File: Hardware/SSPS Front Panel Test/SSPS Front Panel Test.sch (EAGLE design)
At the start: 81 parts, among them J1 61400413321, SW1 B3W-9000-RG2C, SW2 B3W-9000-RG2C, U1 P8X32A-Q44, U10 STP16CP05XTTR, U11 FT230XS, U12 IP4234CZ6, U2 STP16CP05XTTR, U3 STP16CP05XTTR, U4 STP16CP05XTTR, U5 STP16CP05XTTR, U6 STP16CP05XTTR, U7 AP1084D25G-13, U8 AP1084D33G-13, U9 STP16CP05XTTR

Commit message: Test for Front Panel of SSPS complete.
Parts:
- removed DISP21: CU16025-UWJ6, PP_Displays:CU16025-UWJ6
- removed H1, H2, H3, H4: MOUNT_HOLE150MIL, PP_Connectors:MOUNT_HOLE150MIL
- added 5V: 5000, PP_Connectors:TEST_POINT_SINGLE_KEYSTONE_5115-5119
- added C17, C18, C19, C20, C21, C22, C23: .1uF, PP_Passives:CAPACITOR_NON_POLAR_0603
- added C24, C25, C26: 0.1uF, PP_Passives:CAPACITOR_NON_POLAR_0603
- added FID1, FID2: FIDUCIAL_100MIL, MF_Aesthetics:FIDUCIAL_100MIL
- added FRAME1: MF_FRAMEDEFAULT, MF_Aesthetics:MF_FRAMEDEFAULT
- added GND: 5001, PP_Connectors:TEST_POINT_SINGLE_KEYSTONE_5115-5119
- added J2: (no value), PP_Connectors:CON_01X08_2.54MM_PIN_HEADER
- added LCD1: CU16025-UW6J, PP_Displays:CU16025-UWJ6
- added R12, R13, R14, R16, R17, R18, R19, R20, R21, R22: 10K, PP_Passives:RESISTOR_0603
- added R15: 1K, PP_Passives:RESISTOR_0603
- added SW3: 5501, PP_Electromechanical:5501
- added U13: FT234XD-R, PP_DigitalIC:FT234XD
- added U14: STP16CP05XTTR, PP_DigitalIC:STP16CP05XTTR
- added X1: ABMM-6.000MHZ-B2-T, MF_Frequency_Control:XTL_7MMX5MM
- U1: value P8X32A-Q44 -> P8X32A-M44; device MF_IC_Digital:P8X32A-Q44 -> PP_DigitalIC:P8X32A-M44
- U11: value FT230XS -> CAT24C512WI-GT3; device MF_IC_Digital:FT230XS -> PP_DigitalIC:EEPROM_I2CSOIC-8_W
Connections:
- removed net RX_LED: U11.CBUS1
- removed net TX_LED: U11.CBUS0
- new net DISP9_DATA: U14.SDO
- new net ENCODER_A: C25.1, R18.2, U1.P7
- new net ENCODER_B: C26.1, R19.1, U1.P6
- new net LCD_SCK: LCD1.SCK, U1.P2
- new net LCD_SI/SO: LCD1.SI/SO, U1.P0
- new net LCD_STB: LCD1.STB, U1.P1
- new net N$39: R15.2, U14.R-EXT
- new net N$40: EN1.1, U14.!OUT0
- new net N$41: EN1.2, U14.!OUT1
- new net N$42: EN1.4, U14.!OUT2
- new net N$43: SW1.CATHODE_1, U14.!OUT3
- new net N$44: SW1.CATHODE_2, U14.!OUT4
- new net N$45: SW2.CATHODE_1, U14.!OUT5
- new net N$46: SW2.CATHODE_2, U14.!OUT6
- new net N$47: SW3.CATHODE_1, U14.!OUT7
- new net N$48: SW3.CATHODE_2, U14.!OUT8
- new net N$49: R20.2, SW1.3
- new net N$50: R21.2, SW2.3
- new net N$54: R22.2, SW3.2
- new net P11: J2.1, U1.P11
- new net P12: J2.2, U1.P12
- new net P13: J2.3, U1.P13
- new net P14: J2.4, U1.P14
- new net P15: J2.5, U1.P15
- new net P16: J2.6, U1.P16
- new net P17: J2.7, U1.P17
- new net P18: J2.8, U1.P18
- new net P19: U1.P19
- new net P20: U1.P20
- new net P21: U1.P21
- new net P22: U1.P22
- new net P23: U1.P23
- new net P24: U1.P24
- new net P25: U1.P25
- new net P26: U1.P26
- new net P27: U1.P27
- new net RES: C21.1, R14.1, U1.!RES
- new net SCL: R12.1, U1.P28, U11.SCL
- new net SDA: R13.1, U1.P29, U11.SDA
- new net SW_1: SW1.4, U1.P8
- new net SW_2: SW2.4, U1.P9
- new net SW_3: SW3.3, U1.P10
- new net TERMINAL_A: EN1.A, R16.1, R18.1
- new net TERMINAL_B: EN1.B, R17.1, R19.2
- new net USB_RST: C21.2
- new net X0: U1.X0, X1.X1
- new net X1: U1.X1, X1.X0
- net 2.5V: now also EN1.5, SW1.ANODE_1, SW1.ANODE_2, SW2.ANODE_1, SW2.ANODE_2, SW3.ANODE_1, SW3.ANODE_2
- net 3.3V: now also C17.2, C18.2, C19.2, C20.2, C22.2, C23.2, C24.1, R12.2, R13.2, R14.2, R16.2, R17.2, R20.1, R21.1, R22.1, U1.VDD, U13.VCC, U14.VDD
- net 3V3OUT: now also U13.3V3OUT, U13.RESET#, U13.VCCIO; no longer U11.!RESET, U11.3V3OUT, U11.VCCIO
- net DISP1_DATA: now also U1.P5
- net DISP8_DATA: now also U14.SDI
- net DISPX_CLK: now also U1.P3, U14.CLK
- net DISPX_LAT: now also U1.P4, U14.LE/DM1
- net GND: now also C17.1, C18.1, C19.1, C20.1, C22.1, C23.1, C24.2, C25.2, C26.2, EN1.C, GND.P$1, LCD1.GND2, R15.1, SW1.1, SW2.1, SW3.1A, U1.!BOE, U1.VSS, U11.A0, U11.A1, U11.A2, U11.WP, U13.GND, U14.!OE/DM2, U14.VSS/GND, X1.GND
- net N$34: now also U13.USBDM; no longer U11.USBDM
- net N$36: now also U13.USBDP; no longer U11.USBDP
- net RX: now also U1.P30, U13.RXD; no longer U11.RXD
- net TX: now also U1.P31, U13.TXD; no longer U11.TXD
- net USB_!RST: now also U13.RTS#; no longer U11.!RTS
- net VBUS_SENSE: now also U13.CBUS0; no longer U11.CBUS3
- net VIN: now also 5V.P$1, LCD1.VCC2
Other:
- moved on the sheet: EN1, SW1, SW2, U1

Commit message: Fixed part numbers.
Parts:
- DISP2, DISP3, DISP4, DISP5: value PSA08-11GWA -> PSA08-11SRWA
- SW3: value 5501 -> 5501M112
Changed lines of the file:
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@@
 <grid distance="0.1" unitdist="inch" unit="inch" style="lines" multiple="1" display="no" altdistance="0.01" altunitdist="inch" altunit="inch"/>
 <layers>
-<layer number="1" name="Top" color="4" fill="1" visible="yes" active="no"/>
-<layer number="2" name="Route2" color="1" fill="3" visible="yes" active="no"/>
-<layer number="3" name="Route3" color="4" fill="3" visible="yes" active="no"/>
-<layer number="4" name="Route4" color="1" fill="4" visible="yes" active="no"/>
-<layer number="5" name="Route5" color="4" fill="4" visible="yes" active="no"/>
-<layer number="6" name="Route6" color="1" fill="8" visible="yes" active="no"/>
-<layer number="7" name="Route7" color="4" fill="8" visible="yes" active="no"/>
-<layer number="8" name="Route8" color="1" fill="2" visible="yes" active="no"/>
-<layer number="9" name="Route9" color="4" fill="2" visible="yes" active="no"/>
-<layer number="10" name="Route10" color="1" fill="7" visible="yes" active="no"/>
-<layer number="11" name="Route11" color="4" fill="7" visible="yes" active="no"/>
-<layer number="12" name="Route12" color="1" fill="5" visible="yes" active="no"/>
-<layer number="13" name="Route13" color="4" fill="5" visible="yes" active="no"/>
-<layer number="14" name="Route14" color="1" fill="6" visible="yes" active="no"/>
-<layer number="15" name="Route15" color="4" fill="6" visible="yes" active="no"/>
-<layer number="16" name="Bottom" color="1" fill="1" visible="yes" active="no"/>
-<layer number="17" name="Pads" color="2" fill="1" visible="yes" active="no"/>
-<layer number="18" name="Vias" color="2" fill="1" visible="yes" active="no"/>
-<layer number="19" name="Unrouted" color="6" fill="1" visible="yes" active="no"/>
-<layer number="20" name="Dimension" color="15" fill="1" visible="yes" active="no"/>
-<layer number="21" name="tPlace" color="7" fill="1" visible="yes" active="no"/>
-<layer number="22" name="bPlace" color="7" fill="1" visible="yes" active="no"/>
-<layer number="23" name="tOrigins" color="15" fill="1" visible="yes" active="no"/>
-<layer number="24" name="bOrigins" color="15" fill="1" visible="yes" active="no"/>
-<layer number="25" name="tNames" color="7" fill="1" visible="yes" active="no"/>
-<layer number="26" name="bNames" color="7" fill="1" visible="yes" active="no"/>
-<layer number="27" name="tValues" color="7" fill="1" visible="yes" active="no"/>
-<layer number="28" name="bValues" color="7" fill="1" visible="yes" active="no"/>
+<layer number="1" name="Top" color="4" fill="1" visible="no" active="no"/>
+<layer number="2" name="Route2" color="1" fill="3" visible="no" active="no"/>
+<layer number="3" name="Route3" color="4" fill="3" visible="no" active="no"/>
+<layer number="4" name="Route4" color="1" fill="4" visible="no" active="no"/>
+<layer number="5" name="Route5" color="4" fill="4" visible="no" active="no"/>
+<layer number="6" name="Route6" color="1" fill="8" visible="no" active="no"/>
+<layer number="7" name="Route7" color="4" fill="8" visible="no" active="no"/>
+<layer number="8" name="Route8" color="1" fill="2" visible="no" active="no"/>
+<layer number="9" name="Route9" color="4" fill="2" visible="no" active="no"/>
+<layer number="10" name="Route10" color="1" fill="7" visible="no" active="no"/>
+<layer number="11" name="Route11" color="4" fill="7" visible="no" active="no"/>
+<layer number="12" name="Route12" color="1" fill="5" visible="no" active="no"/>
+<layer number="13" name="Route13" color="4" fill="5" visible="no" active="no"/>
+<layer number="14" name="Route14" color="1" fill="6" visible="no" active="no"/>
+<layer number="15" name="Route15" color="4" fill="6" visible="no" active="no"/>
+<layer number="16" name="Bottom" color="1" fill="1" visible="no" active="no"/>
+<layer number="17" name="Pads" color="2" fill="1" visible="no" active="no"/>
+<layer number="18" name="Vias" color="2" fill="1" visible="no" active="no"/>
+<layer number="19" name="Unrouted" color="6" fill="1" visible="no" active="no"/>
+<layer number="20" name="Dimension" color="15" fill="1" visible="no" active="no"/>
+<layer number="21" name="tPlace" color="7" fill="1" visible="no" active="no"/>
+<layer number="22" name="bPlace" color="7" fill="1" visible="no" active="no"/>
+<layer number="23" name="tOrigins" color="15" fill="1" visible="no" active="no"/>
+<layer number="24" name="bOrigins" color="15" fill="1" visible="no" active="no"/>
+<layer number="25" name="tNames" color="7" fill="1" visible="no" active="no"/>
+<layer number="26" name="bNames" color="7" fill="1" visible="no" active="no"/>
+<layer number="27" name="tValues" color="7" fill="1" visible="no" active="no"/>
+<layer number="28" name="bValues" color="7" fill="1" visible="no" active="no"/>
 <layer number="29" name="tStop" color="7" fill="3" visible="no" active="no"/>
 <layer number="30" name="bStop" color="7" fill="6" visible="no" active="no"/>
@@
 <layer number="35" name="tGlue" color="7" fill="4" visible="no" active="no"/>
 <layer number="36" name="bGlue" color="7" fill="5" visible="no" active="no"/>
-<layer number="37" name="tTest" color="7" fill="1" visible="yes" active="no"/>
-<layer number="38" name="bTest" color="7" fill="1" visible="yes" active="no"/>
+<layer number="37" name="tTest" color="7" fill="1" visible="no" active="no"/>
+<layer number="38" name="bTest" color="7" fill="1" visible="no" active="no"/>
 <layer number="39" name="tKeepout" color="4" fill="11" visible="no" active="no"/>
 <layer number="40" name="bKeepout" color="1" fill="11" visible="no" active="no"/>
@@
 <layer number="44" name="Drills" color="7" fill="1" visible="no" active="no"/>
 <layer number="45" name="Holes" color="7" fill="1" visible="no" active="no"/>
-<layer number="46" name="Milling" color="3" fill="1" visible="yes" active="no"/>
-<layer number="47" name="Measures" color="7" fill="1" visible="yes" active="no"/>
-<layer number="48" name="Document" color="7" fill="1" visible="yes" active="no"/>
-<layer number="49" name="Reference" color="7" fill="1" visible="yes" active="no"/>
-<layer number="50" name="dxf" color="7" fill="1" visible="yes" active="no"/>
-<layer number="51" name="tDocu" color="7" fill="1" visible="yes" active="no"/>
-<layer number="52" name="bDocu" color="7" fill="1" visible="yes" active="no"/>
-<layer number="53" name="tGND_GNDA" color="7" fill="9" visible="yes" active="no"/>
-<layer number="54" name="bGND_GNDA" color="1" fill="9" visible="yes" active="no"/>
-<layer number="56" name="wert" color="7" fill="1" visible="yes" active="no"/>
+<layer number="46" name="Milling" color="3" fill="1" visible="no" active="no"/>
+<layer number="47" name="Measures" color="7" fill="1" visible="no" active="no"/>
+<layer number="48" name="Document" color="7" fill="1" visible="no" active="no"/>
+<layer number="49" name="Reference" color="7" fill="1" visible="no" active="no"/>
+<layer number="50" name="dxf" color="7" fill="1" visible="no" active="no"/>
+<layer number="51" name="tDocu" color="7" fill="1" visible="no" active="no"/>
+<layer number="52" name="bDocu" color="7" fill="1" visible="no" active="no"/>
+<layer number="53" name="tGND_GNDA" color="7" fill="9" visible="no" active="no"/>
+<layer number="54" name="bGND_GNDA" color="1" fill="9" visible="no" active="no"/>
+<layer number="56" name="wert" color="7" fill="1" visible="no" active="no"/>
 <layer number="91" name="Nets" color="2" fill="1" visible="yes" active="yes"/>
 <layer number="92" name="Busses" color="1" fill="1" visible="yes" active="yes"/>
@@
 <parts>
 <part name="DISP1" library="PP_LED" deviceset="PSA08-11SRWA" device="" value="PSA08-11SRWA"/>
-<part name="DISP2" library="PP_LED" deviceset="PSA08-11SRWA" device="" value="PSA08-11GWA"/>
-<part name="DISP3" library="PP_LED" deviceset="PSA08-11SRWA" device="" value="PSA08-11GWA"/>
-<part name="DISP4" library="PP_LED" deviceset="PSA08-11SRWA" device="" value="PSA08-11GWA"/>
+<part name="DISP2" library="PP_LED" deviceset="PSA08-11SRWA" device="" value="PSA08-11SRWA"/>
+<part name="DISP3" library="PP_LED" deviceset="PSA08-11SRWA" device="" value="PSA08-11SRWA"/>
+<part name="DISP4" library="PP_LED" deviceset="PSA08-11SRWA" device="" value="PSA08-11SRWA"/>
 <part name="D1" library="PP_LED" deviceset="LED_SINGLE" device="_WP1043" value="WP1043ID"/>
 <part name="D2" library="PP_LED" deviceset="LED_SINGLE" device="_WP1043" value="WP1043ID"/>
@@
 <part name="D7" library="PP_LED" deviceset="LED_SINGLE" device="_WP1043" value="WP1043YD"/>
 <part name="D8" library="PP_LED" deviceset="LED_SINGLE" device="_WP1043" value="WP1043YD"/>
-<part name="DISP5" library="PP_LED" deviceset="PSA08-11SRWA" device="" value="PSA08-11GWA"/>
+<part name="DISP5" library="PP_LED" deviceset="PSA08-11SRWA" device="" value="PSA08-11SRWA"/>
 <part name="D9" library="PP_LED" deviceset="LED_SINGLE" device="_WP1043" value="WP1043YD"/>
 <part name="D10" library="PP_LED" deviceset="LED_SINGLE" device="_WP1043" value="WP1043YD"/>
@@
 <part name="5V" library="PP_Connectors" deviceset="TEST_POINT_SINGLE" device="_KEYSTONE_5115-5119" value="5000"/>
 <part name="GND" library="PP_Connectors" deviceset="TEST_POINT_SINGLE" device="_KEYSTONE_5115-5119" value="5001"/>
-<part name="SW3" library="PP_Electromechanical" deviceset="5501" device="" value="5501"/>
+<part name="SW3" library="PP_Electromechanical" deviceset="5501" device="" value="5501M112"/>
 <part name="U14" library="PP_DigitalIC" deviceset="STP16CP05" device="XTTR" value="STP16CP05XTTR"/>
 <part name="U$26" library="MF_Aesthetics" deviceset="GND_RAIL" device="" value="GND"/>

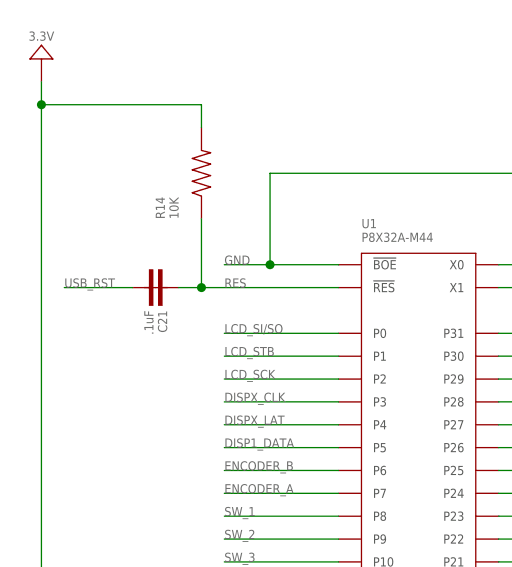
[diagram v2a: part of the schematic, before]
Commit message: Fixed USB_!RST net...
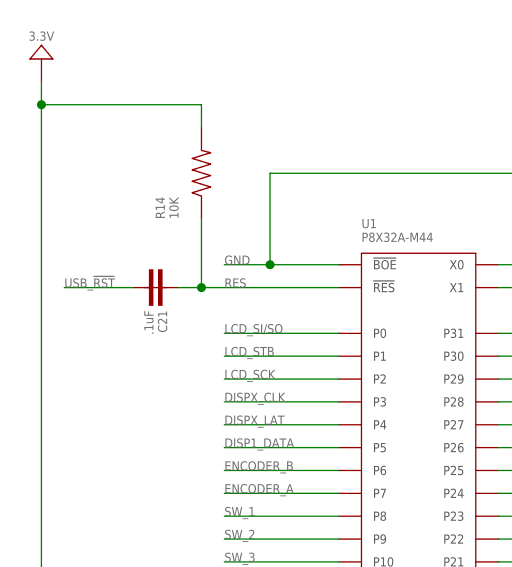
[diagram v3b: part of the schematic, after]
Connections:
- removed net USB_RST: C21.2
- net USB_!RST: now also C21.2
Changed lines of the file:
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@@
 <pinref part="U13" gate="G$1" pin="RTS#"/>
+</segment>
+<segment>
+<pinref part="C21" gate="G$1" pin="2"/>
+<wire x1="73.66" y1="-81.28" x2="66.04" y2="-81.28" width="0.1524" layer="91"/>
+<label x="66.04" y="-81.28" size="1.016" layer="95" font="vector"/>
 </segment>
 </net>
@@
 </segment>
 </net>
-<net name="USB_RST" class="0">
-<segment>
-<pinref part="C21" gate="G$1" pin="2"/>
-<wire x1="73.66" y1="-81.28" x2="66.04" y2="-81.28" width="0.1524" layer="91"/>
-<label x="66.04" y="-81.28" size="1.016" layer="95" font="vector"/>
-</segment>
-</net>

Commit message: SSPS Front Panel Test fixed.
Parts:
- FRAME1: REVNUM REV: 1 -> REV: 2
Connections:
- net 2.5V: no longer EN1.5
- net 3.3V: now also EN1.5
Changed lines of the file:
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@@
 <part name="FRAME1" library="MF_Aesthetics" deviceset="MF_FRAME" device="DEFAULT">
 <attribute name="DNAME" value="PARKER DILLMANN"/>
-<attribute name="REVNUM" value="REV: 1"/>
+<attribute name="REVNUM" value="REV: 2"/>
 </part>
 <part name="FID1" library="MF_Aesthetics" deviceset="FIDUCIAL" device="_100MIL"/>
@@
 <pinref part="R20" gate="G$1" pin="1"/>
 <wire x1="449.58" y1="-157.48" x2="447.04" y2="-157.48" width="0.1524" layer="91"/>
-<wire x1="447.04" y1="-157.48" x2="447.04" y2="-101.6" width="0.1524" layer="91"/>
+<wire x1="447.04" y1="-157.48" x2="447.04" y2="-119.38" width="0.1524" layer="91"/>
 <pinref part="U$33" gate="G$1" pin="P$1"/>
 <pinref part="R21" gate="G$1" pin="1"/>
+<wire x1="447.04" y1="-119.38" x2="447.04" y2="-101.6" width="0.1524" layer="91"/>
 <wire x1="449.58" y1="-185.42" x2="447.04" y2="-185.42" width="0.1524" layer="91"/>
 <wire x1="447.04" y1="-185.42" x2="447.04" y2="-157.48" width="0.1524" layer="91"/>
@@
 <wire x1="447.04" y1="-213.36" x2="447.04" y2="-185.42" width="0.1524" layer="91"/>
 <junction x="447.04" y="-185.42"/>
+<pinref part="EN1" gate="G$1" pin="5"/>
+<wire x1="464.82" y1="-119.38" x2="447.04" y2="-119.38" width="0.1524" layer="91"/>
+<junction x="447.04" y="-119.38"/>
 </segment>
 </net>
@@
 <pinref part="SW1" gate="G$1" pin="ANODE_1"/>
 <wire x1="477.52" y1="-167.64" x2="490.22" y2="-167.64" width="0.1524" layer="91"/>
-<wire x1="490.22" y1="-167.64" x2="490.22" y2="-104.14" width="0.1524" layer="91"/>
+<wire x1="490.22" y1="-167.64" x2="490.22" y2="-101.6" width="0.1524" layer="91"/>
 <pinref part="SW1" gate="G$1" pin="ANODE_2"/>
-<wire x1="490.22" y1="-104.14" x2="490.22" y2="-101.6" width="0.1524" layer="91"/>
 <wire x1="477.52" y1="-175.26" x2="490.22" y2="-175.26" width="0.1524" layer="91"/>
 <wire x1="490.22" y1="-175.26" x2="490.22" y2="-167.64" width="0.1524" layer="91"/>
@@
 <junction x="490.22" y="-167.64"/>
 <pinref part="U$28" gate="G$1" pin="P$1"/>
-<wire x1="490.22" y1="-104.14" x2="441.96" y2="-104.14" width="0.1524" layer="91"/>
-<pinref part="EN1" gate="G$1" pin="5"/>
-<wire x1="441.96" y1="-104.14" x2="441.96" y2="-119.38" width="0.1524" layer="91"/>
-<wire x1="441.96" y1="-119.38" x2="464.82" y2="-119.38" width="0.1524" layer="91"/>
-<junction x="490.22" y="-104.14"/>
-</segment>
-</net>
+</segment>
+</net>
